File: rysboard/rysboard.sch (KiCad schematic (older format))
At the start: 8 parts, among them J1 RPi4, J17 Conn_01x03, J18 Conn_01x05, U4 STM32G030K8Tx

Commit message: Added eval board for STM32G031K8U6, rybsoard layout done, exact vals yet to be calculated
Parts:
- removed U4: STM32G030K8Tx, Package_QFP:LQFP-32_7x7mm_P0.8mm, symbol rysboard:STM32G030K8Tx
- added U4: STM32G031K8Ux, Package_DFN_QFN:QFN-32-1EP_5x5mm_P0.5mm_EP3.45x3.45mm, symbol rysboard:STM32G031K8Ux
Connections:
- wire segments 115 -> 116
- no-connect marks 4 -> 9
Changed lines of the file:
@@
 Text Label 950  3200 0    50   ~ 0
 MOTOR_BUSY
-Wire Wire Line
-	8250 1775 7675 1775
-Text Label 7675 1775 0    50   ~ 0
+Text Label 7700 1800 0    50   ~ 0
 MOTOR_FLAG
-Wire Wire Line
-	8250 1575 7675 1575
-Text Label 7675 1575 0    50   ~ 0
+Text Label 7700 1600 0    50   ~ 0
 ~MOTOR_STBY
-Wire Wire Line
-	8250 1675 7675 1675
-Text Label 7675 1675 0    50   ~ 0
+Text Label 7700 1700 0    50   ~ 0
 MOTOR_BUSY
-Wire Wire Line
-	9225 1575 9675 1575
-Text Label 9675 1575 2    50   ~ 0
+Text Label 9650 1600 2    50   ~ 0
 SPI_MISO
-Wire Wire Line
-	9225 1675 9675 1675
-Text Label 9675 1675 2    50   ~ 0
+Text Label 9650 1700 2    50   ~ 0
 SPI_MOSI
-Wire Wire Line
-	9225 1775 9675 1775
-Text Label 9675 1775 2    50   ~ 0
+Text Label 9650 1800 2    50   ~ 0
 SPI_CLK
-Wire Wire Line
-	9225 1875 9675 1875
-Text Label 9675 1875 2    50   ~ 0
+Text Label 9650 1900 2    50   ~ 0
 ~SPI_CS0
 Text Label 7775 3450 0    50   ~ 0
@@
 Text Label 950  3000 0    50   ~ 0
 SPI_IRQEXT
-$Sheet
-S 8250 1500 975  600
-U 5EB7428E
-F0 "Motor Drivers" 50
-F1 "motor_drivers.sch" 50
-F2 "~STBY" I L 8250 1575 50
-F3 "~SPI_CS" I R 9225 1875 50
-F4 "SPI_CLK" I R 9225 1775 50
-F5 "SPI_MISO" O R 9225 1575 50
-F6 "SPI_MOSI" I R 9225 1675 50
-F7 "BUSY" O L 8250 1675 50
-F8 "FLAG" O L 8250 1775 50
-$EndSheet
 $Comp
 L power:PWR_FLAG #FLG0103
@@
 NoConn ~ 1500 2900
 NoConn ~ 1500 2800
-$Comp
-L rysboard:STM32G030K8Tx U4
-U 1 1 6035F242
-P 2350 6050
-F 0 "U4" H 2300 6250 50  0000 C CNN
-F 1 "STM32G030K8Tx" H 2250 6600 50  0000 C CNN
-F 2 "Package_QFP:LQFP-32_7x7mm_P0.8mm" H 3050 4650 50  0001 R CNN
-F 3 "http://www.st.com/st-web-ui/static/active/en/resource/technical/document/datasheet/DM00088500.pdf" H 2350 6050 50  0001 C CNN
-	1    2350 6050
-	1    0    0    -1
-$EndComp
 Text GLabel 2300 4950 0    50   Input ~ 0
 MCU_3.3V
@@
 Wire Wire Line
 	8250 5100 7300 5100
+$Comp
+L rysboard:STM32G031K8Ux U4
+U 1 1 6039ADD9
+P 2350 6050
+F 0 "U4" H 2350 6000 50  0000 C CNN
+F 1 "STM32G031K8Ux" H 2200 6600 50  0000 C CNN
+F 2 "Package_DFN_QFN:QFN-32-1EP_5x5mm_P0.5mm_EP3.45x3.45mm" H 3050 4650 50  0001 R CNN
+F 3 "http://www.st.com/st-web-ui/static/active/en/resource/technical/document/datasheet/DM00088500.pdf" H 2350 6050 50  0001 C CNN
+	1    2350 6050
+	1    0    0    -1
+$EndComp
+NoConn ~ 2850 6850
+NoConn ~ 2850 6550
+NoConn ~ 2850 6450
+NoConn ~ 1750 6750
+NoConn ~ 1750 6250
+Text Label 7200 1900 0    50   ~ 0
+ENABLE_STEPPER_MOTORS
+$Sheet
+S 8250 1500 1000 600
+U 5EB7428E
+F0 "Motor Drivers" 50
+F1 "motor_drivers.sch" 50
+F2 "~STBY" I L 8250 1600 50
+F3 "~SPI_CS" I R 9250 1900 50
+F4 "SPI_CLK" I R 9250 1800 50
+F5 "SPI_MISO" O R 9250 1600 50
+F6 "SPI_MOSI" I R 9250 1700 50
+F7 "BUSY" O L 8250 1700 50
+F8 "FLAG" O L 8250 1800 50
+F9 "MOT_EN" I L 8250 1900 50
+$EndSheet
+Wire Wire Line
+	7700 1600 8250 1600
+Wire Wire Line
+	8250 1700 7700 1700
+Wire Wire Line
+	7700 1800 8250 1800
+Wire Wire Line
+	7200 1900 8250 1900
+Wire Wire Line
+	9250 1600 9650 1600
+Wire Wire Line
+	9650 1700 9250 1700
+Wire Wire Line
+	9650 1800 9250 1800
+Wire Wire Line
+	9650 1900 9250 1900
 $EndSCHEMATC

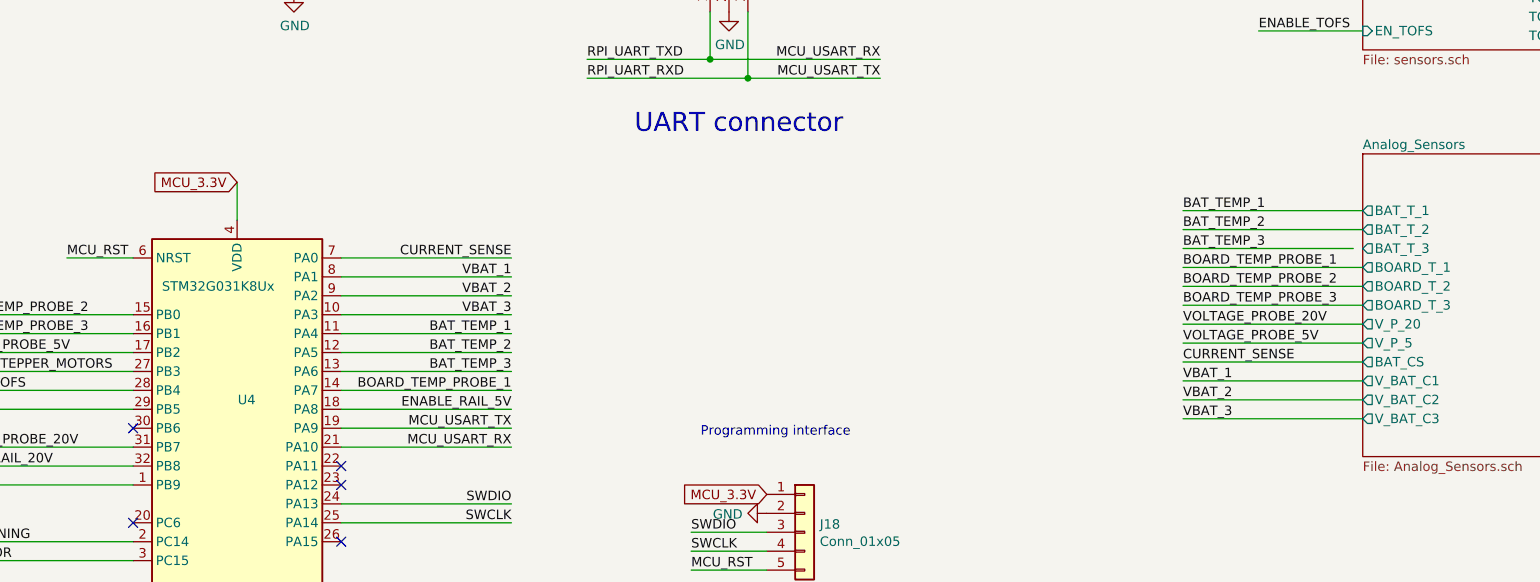
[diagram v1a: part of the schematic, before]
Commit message: sensors enable added, Vref problem to solve
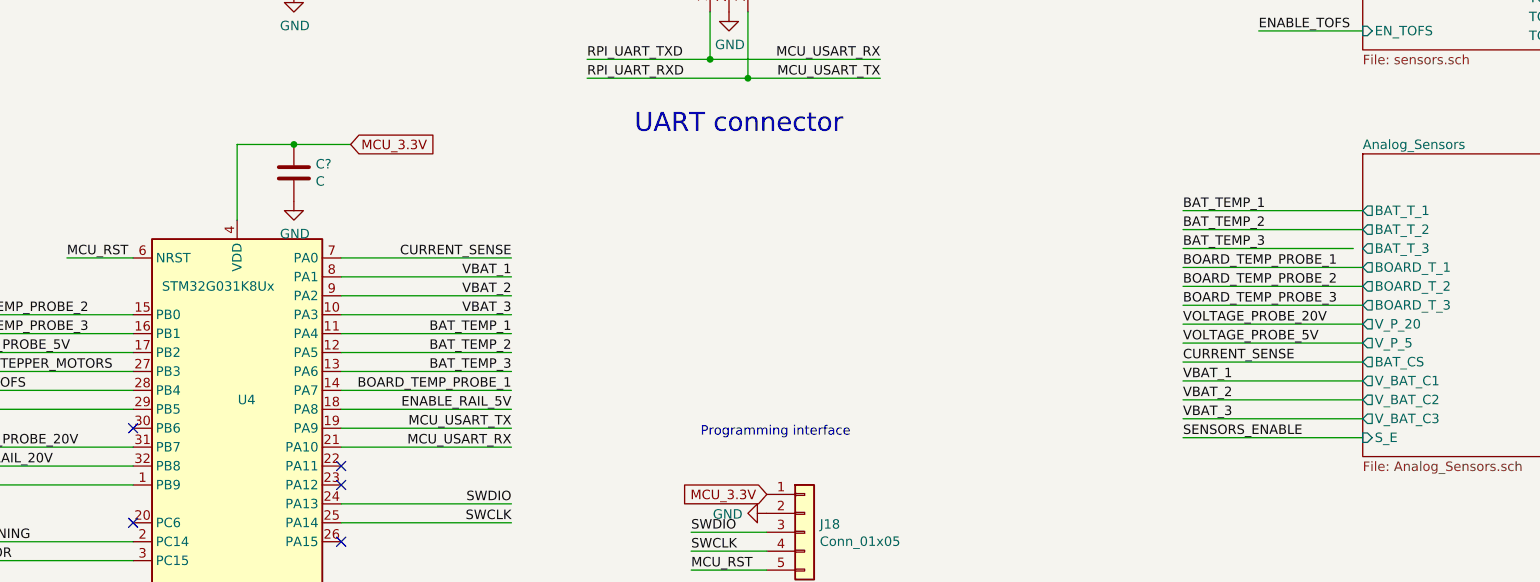
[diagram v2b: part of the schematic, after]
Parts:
- added C?: C, symbol Device:C
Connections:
- net GND: now also C?.2
- net MCU_3.3V: now also C?.1
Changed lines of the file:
@@
 NoConn ~ 1500 2900
 NoConn ~ 1500 2800
-Text GLabel 2300 4950 0    50   Input ~ 0
+Text GLabel 2900 4750 2    50   Input ~ 0
 MCU_3.3V
-Wire Wire Line
-	2300 4950 2300 5150
 Wire Wire Line
 	1900 3800 2000 3800
@@
 F12 "V_BAT_C2" O L 8250 6100 50
 F13 "V_BAT_C3" O L 8250 6200 50
+F14 "S_E" I L 8250 6300 50
 $EndSheet
 Text Label 7300 5500 0    50   ~ 0
@@
 Wire Wire Line
 	9650 1900 9250 1900
+Text Label 7300 6300 0    50   ~ 0
+SENSORS_ENABLE
+Wire Wire Line
+	7300 6300 8250 6300
+$Comp
+L Device:C C?
+U 1 1 603CCD3F
+P 2600 4900
+F 0 "C?" H 2715 4946 50  0000 L CNN
+F 1 "C" H 2715 4855 50  0000 L CNN
+F 2 "" H 2638 4750 50  0001 C CNN
+F 3 "~" H 2600 4900 50  0001 C CNN
+	1    2600 4900
+	1    0    0    -1
+$EndComp
+Wire Wire Line
+	2900 4750 2600 4750
+Wire Wire Line
+	2300 4750 2300 5150
+Connection ~ 2600 4750
+Wire Wire Line
+	2600 4750 2300 4750
+$Comp
+L power:GND #PWR?
+U 1 1 603D4B7E
+P 2600 5050
+F 0 "#PWR?" H 2600 4800 50  0001 C CNN
+F 1 "GND" H 2605 4877 50  0000 C CNN
+F 2 "" H 2600 5050 50  0001 C CNN
+F 3 "" H 2600 5050 50  0001 C CNN
+	1    2600 5050
+	1    0    0    -1
+$EndComp
 $EndSCHEMATC
